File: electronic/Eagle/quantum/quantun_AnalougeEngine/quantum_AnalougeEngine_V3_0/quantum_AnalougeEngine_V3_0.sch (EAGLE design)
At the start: 258 parts, among them IC1 OP275, IC2 OP275, IC3 OP275, IC4 OP275, IC6 OP275, IC8 OP275, IC9 TL072, K5 RELAY_EE2-5NU, K6 RELAY_EE2-5NU, K7 RELAY_EE2-5NU, K8 RELAY_EE2-5NU, Q1 BLM21, U1 ATMEGA2560-16AU, U10 ATMEGA328P-AU, U10_PROG 6PIN_HEADER_SMD_OPEN, U11 ATMEGA328P-AU, U11_PROG 6PIN_HEADER_SMD_OPEN, U12 ULN2003, U1_PROG MAIN_µC, U4 THAT1240, U5 ATMEGA16U2-AU, U5_PROG 6PIN_HEADER_SMD_OPEN, U6 THAT1240, U7 THAT1240, U8 THAT1240

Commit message: minor changes
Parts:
- removed C23, C24, C33, C34, C38, C39, C44, C45, C46: 22pF, C_Sager_Bibliothek:CAPACITOR"
- removed C31, C35, C40, C51: 1uF, C_Sager_Bibliothek:CAPACITOR"
- removed C32, C37, C42, C43, C47, C48, C49, C50, C52, C65, C66: 100nF, C_Sager_Bibliothek:CAPACITOR"
- removed C36, C41: 4,7uF/16V, C_Sager_Bibliothek:SMD_ELCTROLYTIC
- removed CONN1: 10PIN_HEADER_SMD, C_Sager_Bibliothek:10PIN_HEADER_SMD
- removed D10, D11, D12, D13, D14, D9: 4148, C_Sager_Bibliothek:4148
- removed DAC1, DAC2: MCP4922, SPI:MCP4922
- removed F1: FUSE_500 mA, C_Sager_Bibliothek:RESTABLE_FUSE
- removed L, L/M_OUT, M, R, R/S_OUT, S: 0R, C_Sager_Bibliothek:RESISTOR"
- removed Q1: BLM21, C_Sager_Bibliothek:FERITEFERITE
- removed QA1, QA2, QA3, QA4: 16 MHz, C_Sager_Bibliothek:CRYSTAL_SM49
- removed R35, R36, R37, R38, R39, R40: 500R, C_Sager_Bibliothek:RESISTOR"
- removed R41, R42, R43, R44: 1K, C_Sager_Bibliothek:RESISTOR"
- removed R45, R68: 1k, C_Sager_Bibliothek:RESISTOR"
- removed R46, R47: 1M, C_Sager_Bibliothek:RESISTOR"
- removed TP05, TP06, TP27, TP28, TP29, TP30, TP31, TP32, TP33, TP34, TP35: TPTHT, C_Sager_Bibliothek:TPTHT
- removed U10, U11: ATMEGA328P-AU, C_Sager_Bibliothek:ATMEGA328P-AU
- removed U10_PROG, U11_PROG, U5_PROG: 6PIN_HEADER_SMD_OPEN, C_Sager_Bibliothek:6PIN_HEADER_SMD_OPEN
- removed U1_PROG: MAIN_µC, C_Sager_Bibliothek:6PIN_HEADER_SMD_OPEN
- removed U5: ATMEGA16U2-AU, C_Sager_Bibliothek:ATMEGA16U2-AU
- removed UR1: 78, C_Sager_Bibliothek:78
- removed USB1: (no value), C_Sager_Bibliothek:SMARTPRJ_PN61729
- removed V1, V2: CG0603ML, C_Sager_Bibliothek:VARISTORVAR-0603
- added IC5: NE5532D, linear:NE5532D
- added L7, L8: SMD_LED_0603, C_Sager_Bibliothek:SMD_LED_0603
- C59, C64: value 22pF -> 100nF
- D1, D2: value Shotky-CD1206 -> 4148
- IC2, IC3, IC6: value OP275 -> NE5532D; device C_Sager_Bibliothek:OP275 -> linear:NE5532D; SPICEPREFIX (none) -> Z
- R1: value 22R -> 100k; SPICEPREFIX (none) -> R
- R13: value 0R -> 100k
- R15, R3: value 1M -> 0R
- R16, R31: value 10k -> 100k
- R17: SPICEPREFIX (none) -> R
- R19, R24: value 100k -> 0R
- R2: value 22R -> 100k
- R21, R26: value 100k -> 180k
- R30: value 10k -> 180k
- R32, R6: value 1k -> 100k
- R33: value 1M -> 500R
- R34: value 10k -> 500R
- R4: value 1M -> 100k
- R48, R49: value 10k -> 20k
- R5: value 1k -> 180k
- U1: value ATMEGA2560-16AU -> NUCLEO-F429ZI; device C_Sager_Bibliothek:ATMEGA2560-16AU -> NUCLEO-F429ZI:NUCLEO-F429ZI
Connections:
- removed net +5V(ANALOG): C52.2, C65.2, C66.2, DAC1.VDD, DAC2.VDD, R30.2, UR1.VO
- removed net C_D(+): R2.1, USB1.3, V2.1
- removed net C_D(-): R1.1, USB1.2, V1.1
- removed net C_UVCC: F1.1, USB1.1
- removed net D(+): R2.2, U5.D+
- removed net D(-): R1.2, U5.D-
- removed net DAC_REF_VOLTAGE: DAC1.V_REF_A, DAC1.V_REF_B, DAC2.V_REF_A, DAC2.V_REF_B, R30.1, R31.2, TP35.TP
- removed net L/M_OUT_SIGNAL: L/M_OUT.2, TP03.TP, U1.PF4_(ADC4/TCK), U10.PC4, U11.PC4
- removed net MAIN_µC_AREF: C50.1, U1.AREF
- removed net MAIN_µC_PB1(SCK): U1.(SCK/PCINT1)_PB1, U1_PROG.P$3
- removed net MAIN_µC_PB2(MOSI): U1.(MOSI/PCINT2)_PB2, U1_PROG.P$4
- removed net MAIN_µC_PB3(MISO): U1.(MISO/PCINT3)_PB3, U1_PROG.P$1
- removed net MAIN_µC_RESET: C43.1, C46.1, D2.A, R46.1, U1.~RESET, U1_PROG.P$5
- removed net MAIN_µC_RX0: R5.2, TP31.TP, U1.(RXD0/PCINT8)_PE0
- removed net MAIN_µC_RX1: R68.2, U1.(RXD1/INT2)_PD2
- removed net MAIN_µC_RX2: R41.2, TP27.TP, U1.(RXD2)_PH0
- removed net MAIN_µC_RX3: R43.2, TP33.TP, U1.PJ0_(RXD3/PCINT9)
- removed net MAIN_µC_TX0: R6.2, TP32.TP, U1.(TXD0)_PE1
- removed net MAIN_µC_TX1: R32.2, U1.(TXD1/INT3)_PD3
- removed net MAIN_µC_TX2: R42.2, TP28.TP, U1.(TXD2)_PH1
- removed net MAIN_µC_TX3: R44.2, TP34.TP, U1.PJ1_(TXD3/PCINT10)
- removed net MAIN_µC_XTAL1: C44.2, QA4.2, R47.2, U1.XTAL1
- removed net MAIN_µC_XTAL2: C45.2, QA4.1, R47.1, U1.XTAL2
- removed net M_SIGNAL: M.2, TP05.TP, U1.PF2_(ADC2), U10.PC2, U11.PC2
- removed net N$50: D11.C, R24.2, S.1
- removed net N$52: D12.A, D3.C, IC6A.OUT
- removed net N$53: D12.C, L/M_OUT.1, R26.2
- removed net N$54: D13.A, IC6B.-IN, R27.2, R28.1
- removed net N$55: D13.C, D14.A, IC6B.OUT
- removed net N$56: D14.C, R/S_OUT.1, R28.2
- removed net N$63: DAC1.SCK, R36.2
- removed net N$66: DAC1.SDI, R37.2
- removed net N$67: DAC2.CS, R40.2
- removed net N$68: DAC2.SCK, R39.2
- removed net N$69: DAC2.SDI, R38.2
- removed net N$74: C43.2, R45.2, U5./_HWB_/_AIN6_/_T0_/_INT7)_PD7
- removed net R/S_OUT_SIGNAL: R/S_OUT.2, TP04.TP, U1.PF5_(ADC5/TMS), U10.PC5, U11.PC5
- removed net S_SIGNAL: S.2, TP06.TP, U1.PF3_(ADC3), U10.PC3, U11.PC3
- removed net UCAP: C31.2, U5.UCAP
- removed net USB_µC_MISO: U5.PB3_(PDO_/_MISO_/_PCINT3), U5_PROG.P$1
- removed net USB_µC_MOSI: U5.(PDI_/_MOSI_/_PCINT2)_PB2, U5_PROG.P$4
- removed net USB_µC_RESET: D1.A, R4.1, U5.~RESET_(PC1_/_DW), U5_PROG.P$5
- removed net USB_µC_RX: R6.1, U5.(RXD1_/_AIN1_/_INT2)_PD2
- removed net USB_µC_SCK: U5.(SCLK_/_PCINT1)_PB1, U5_PROG.P$3
- removed net USB_µC_TX: R5.1, U5.(TXD1_/_INT3)_PD3
- removed net USB_µC_UGND: C31.1, Q1.2, U5.UGND, USB1.4
- removed net USB_µC_XTAL1: C24.2, QA1.2, R3.2, U5.XTAL1
- removed net USB_µC_XTAL2: C23.2, QA1.1, R3.1, U5.(PC0)_XTAL2
- removed net UVCC: C32.1, F1.2, U5.UVCC
- removed net VCA1_A6: U10.ADC6
- removed net VCA1_A7: U10.ADC7
- removed net VCA1_AREF: C37.2, U10.AREF
- removed net VCA1_D10: U10.PB2
- removed net VCA1_D11(MOSI): R37.1, U10.PB3, U10_PROG.P$4
- removed net VCA1_D12(MISO): U10.PB4, U10_PROG.P$1
- removed net VCA1_D13(SCK): R36.1, U10.PB5, U10_PROG.P$3
- removed net VCA1_D2: R35.1, U10.PD2
- removed net VCA1_D3: U10.PD3
- removed net VCA1_D4: U10.PD4
- removed net VCA1_D5: U10.PD5
- removed net VCA1_D6: U10.PD6
- removed net VCA1_D7: U10.PD7
- removed net VCA1_D8: U10.PB0
- removed net VCA1_D9: U10.PB1
- removed net VCA1_RESET: R16.1, U10.PC6, U10_PROG.P$5
- removed net VCA1_µC_RX: R42.1, U10.PD0
- removed net VCA1_µC_TX: R41.1, U10.PD1
- removed net VCA2_A6: U11.ADC6
- removed net VCA2_A7: U11.ADC7
- removed net VCA2_AREF: C42.2, U11.AREF
- removed net VCA2_D10: U11.PB2
- removed net VCA2_D11(MOSI): R38.1, U11.PB3, U11_PROG.P$4
- removed net VCA2_D12(MISO): U11.PB4, U11_PROG.P$1
- removed net VCA2_D13(SCK): R39.1, U11.PB5, U11_PROG.P$3
- removed net VCA2_D2: R40.1, U11.PD2
- removed net VCA2_D3: U11.PD3
- removed net VCA2_D4: U11.PD4
- removed net VCA2_D5: U11.PD5
- removed net VCA2_D6: U11.PD6
- removed net VCA2_D7: U11.PD7
- removed net VCA2_D8: U11.PB0
- removed net VCA2_D9: U11.PB1
- removed net VCA2_RESET: R34.1, U11.PC6, U11_PROG.P$5
- removed net VCA2_µC_RX: R44.1, U11.PD0
- removed net VCA2_µC_TX: R43.1, U11.PD1
- removed net XTAL1_VCA1: C33.2, QA2.2, R15.2, U10.PB6
- removed net XTAL1_VCA2: C38.2, QA3.2, R33.2, U11.PB6
- removed net XTAL2_VCA1: C34.2, QA2.1, R15.1, U10.PB7
- removed net XTAL2_VCA2: C39.2, QA3.1, R33.1, U11.PB7
- new net N$10: D3.A, R20.1, R22.2
- new net N$3: D4.C, IC2A.-IN, R17.2, R22.1
- new net N$35: IC2B.OUT, R19.1, R23.2
- new net N$37: D8.C, IC3A.-IN, R18.2, R27.1
- new net N$4: D3.C, D4.A, IC2A.OUT
- net +5V: now also L7.+, L8.+; no longer C19.1, C20.1, C35.2, C36.+, C40.2, C41.+, C47.1, C48.1, C49.1, CONN1.P$1, CONN1.P$2, CONN1.P$3, D1.C, D2.C, DAC1.SHDN, DAC2.SHDN, R16.2, R34.2, R4.2, R46.2, U1.AVCC, U1.VCC, U1.VCC_2, U1.VCC_3, U1.VCC_4, U10.AVCC, U10.VCC, U10.VCC_2, U10_PROG.P$2, U11.AVCC, U11.VCC, U11.VCC_2, U11_PROG.P$2, U1_PROG.P$2, U5.AVCC, U5.VCC, U5_PROG.P$2
- net AGND: now also C19.2, C20.2, IC5A.+IN, IC5B.+IN; no longer C51.1, C52.1, C65.1, C66.1, DAC1.VSS, DAC2.VSS, R13.2, R31.1, UR1.GND
- net DAC1_OUT(A): no longer DAC1.V_OUT_A
- net DAC1_OUT(B): no longer DAC1.V_OUT_B
- net DAC2_OUT(A): no longer DAC2.V_OUT_A
- net DAC2_OUT(B): no longer DAC2.V_OUT_B
- net DGND: no longer C19.2, C20.2, C23.1, C24.1, C32.2, C33.1, C34.1, C35.1, C36.-, C37.1, C38.1, C39.1, C40.1, C41.-, C42.1, C44.1, C45.1, C46.2, C47.2, C48.2, C49.2, C50.2, CONN1.P$10, CONN1.P$5, CONN1.P$6, CONN1.P$7, CONN1.P$8, DAC1.LDAC, DAC2.LDAC, R13.1, R45.1, U1.GND, U1.GND_2, U1.GND_3, U1.GND_4, U1.GND_5, U10.GND, U10.GND_2, U10.GND_3, U10_PROG.P$6, U11.GND, U11.GND_2, U11.GND_3, U11_PROG.P$6, U1_PROG.P$6, U5.GND, U5_PROG.P$6
- net L: now also R1.1, R21.1, R5.1
- net L/M_OUT(VCA1_OUT): no longer R25.1
- net L_SIGNAL: now also R19.2, R3.2, TP03.TP; no longer L.2, U1.PF0_(ADC0), U10.PC0, U11.PC0
- net M: no longer R21.1
- net MAIN_µC_D2: no longer U1.(OC3B/INT4)_PE4
- net MAIN_µC_D3: no longer U1.(OC3C/INT5)_PE5
- net MAIN_µC_D4: no longer U1.(OC0B)_PG5
- net MAIN_µC_D5: no longer U1.(OC3A/AIN1)_PE3
- net MAIN_µC_D6: no longer U1.(OC4A)_PH3
- net MAIN_µC_D7: no longer U1.(OC4B)_PH4
- net N$12: now also D1.A, R4.1, R6.2; no longer U1.(OC2A/PCINT4)_PB4
- net N$16: now also L3.-; no longer L2.-
- net N$20: now also IC2B.-IN, R20.2, R21.2, R23.1; no longer D5.C, L.1, R18.2
- net N$26: now also L8.-; no longer L6.-
- net N$29: now also L7.-; no longer L5.-
- net N$30: now also L6.-; no longer L4.-
- net N$32: now also L5.-; no longer L3.-
- net N$34: now also IC5B.-IN, R13.1, R4.2, R5.2; no longer Q1.1, USB1.P$1, USB1.P$2, V1.2, V2.2
- net N$36: now also IC5B.OUT, R13.2, R3.1; no longer DAC1.CS, R35.2
- net N$38: now also D5.C, D8.A, IC3A.OUT; no longer D4.A, IC2A.-IN, R17.2, R18.1
- net N$39: now also R25.1, R27.2; no longer D4.C, IC2A.OUT
- net N$40: now also IC3B.-IN, R25.2, R26.2, R28.1; no longer D6.A, IC2B.-IN, R19.2, R20.1
- net N$41: now also IC3B.OUT, R24.1, R28.2; no longer D6.C, D7.A, IC2B.OUT
- net N$42: now also IC6A.-IN, R2.2, R31.1; no longer R.1, R20.2
- net N$44: now also D6.C, D7.A, IC6A.OUT; no longer D8.A, IC3A.-IN, R21.2, R22.1
- net N$46: now also D6.A, R16.1, R31.2; no longer D8.C, D9.A, IC3A.OUT
- net N$47: now also IC6B.-IN, R16.2, R30.2, R32.1; no longer D9.C, M.1, R22.2
- net N$48: now also IC6B.OUT, R15.1, R32.2; no longer D10.A, IC3B.-IN, R23.2, R24.1
- net N$49: now also L2.-, R33.2; no longer D10.C, D11.A, IC3B.OUT
- net N$51: now also L4.-, R34.2; no longer D3.A, IC6A.-IN, R25.2, R26.1
- net N$6: now also D2.C, IC5A.-IN, R1.2, R6.1; no longer CONN1.P$4, R68.1, TP29.TP
- net N$9: now also D1.C, D2.A, IC5A.OUT; no longer CONN1.P$9, R32.1, TP30.TP
- net OUT1_DRIVER: now also R33.1
- net OUT2_DRIVER: now also R34.1
- net R: now also R18.1, R2.1, R26.1, R30.1; no longer R19.1
- net R/S_OUT(VCA2_OUT): no longer R27.1
- net R_SIGNAL: now also R15.2, R24.2, TP04.TP; no longer R.2, U1.PF1_(ADC1), U10.PC1, U11.PC1
- net S: no longer R23.1
- net V+: now also C20.1, IC5P.V+; no longer C51.2, UR1.VI
- net V-: now also C19.1, IC5P.V-
- net VCA1_EC+: no longer U1.PF7_(ADC7/TDI)
- net VCA2_EC+: no longer U1.PF6_(ADC6/TDO)
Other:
- note added: "Bypass"
- note added: "Präzisionsgleichrichter"

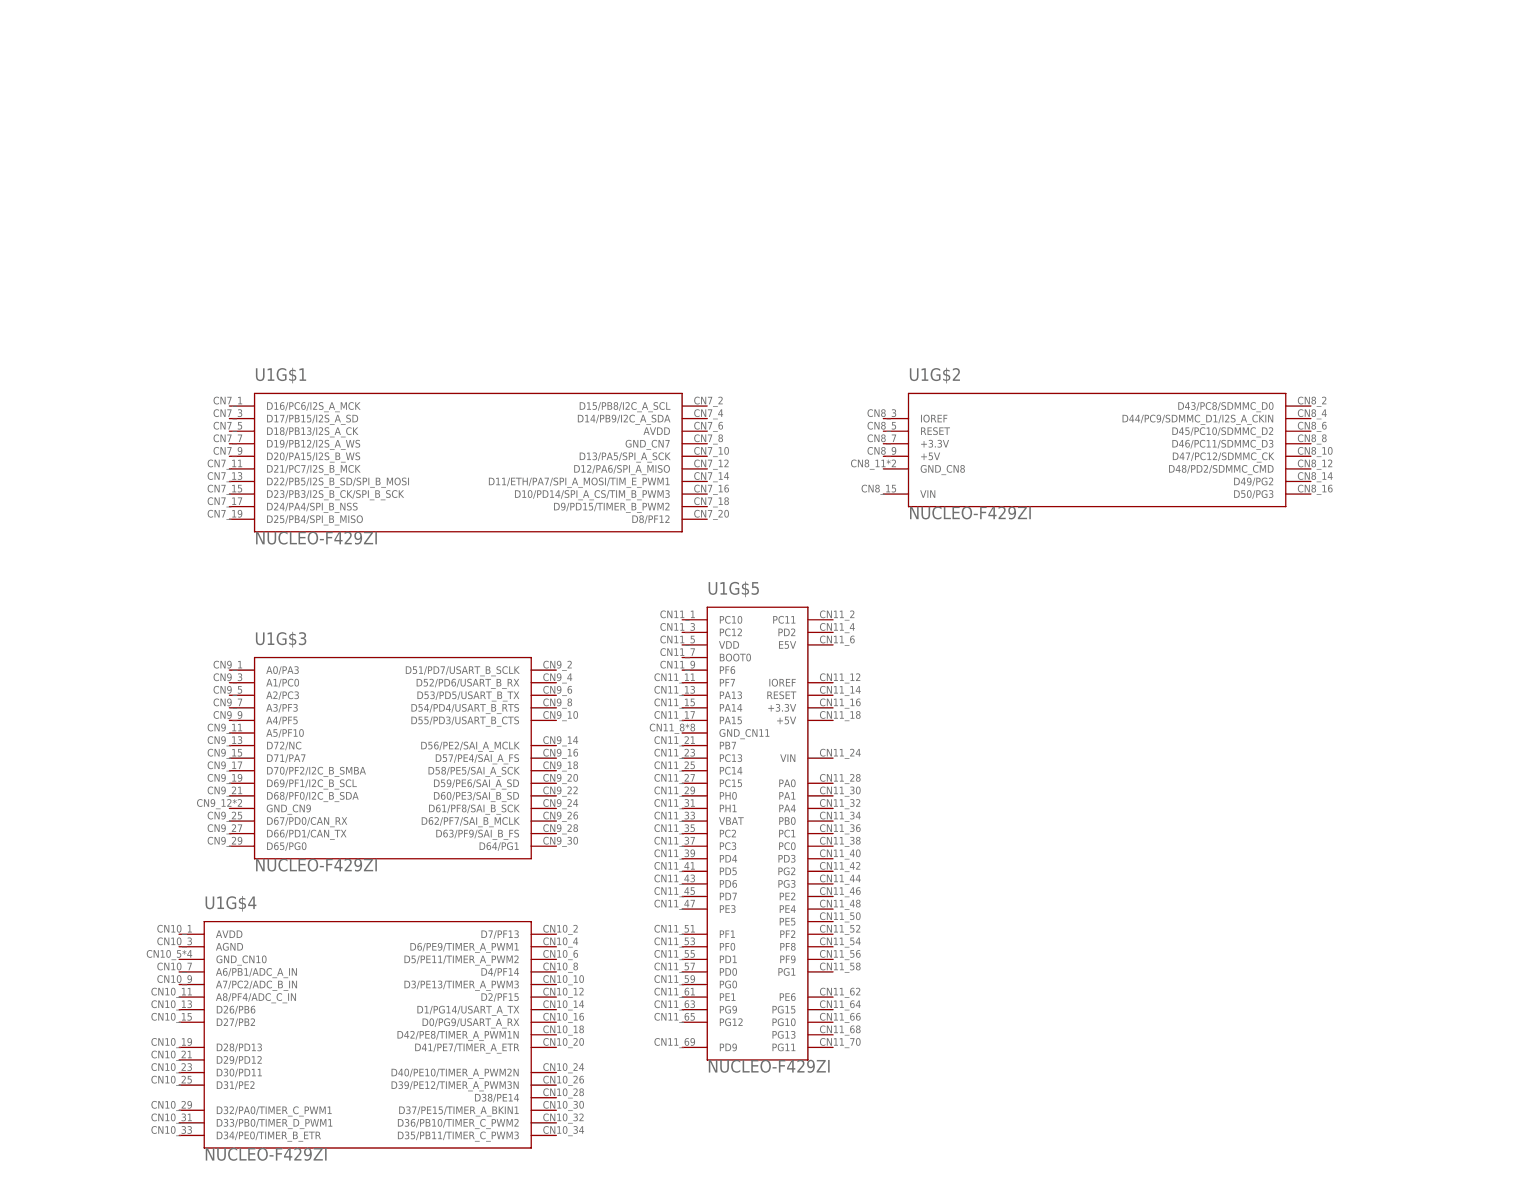
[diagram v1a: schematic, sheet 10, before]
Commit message: Shematic updates + Created MotherEngine.ioc
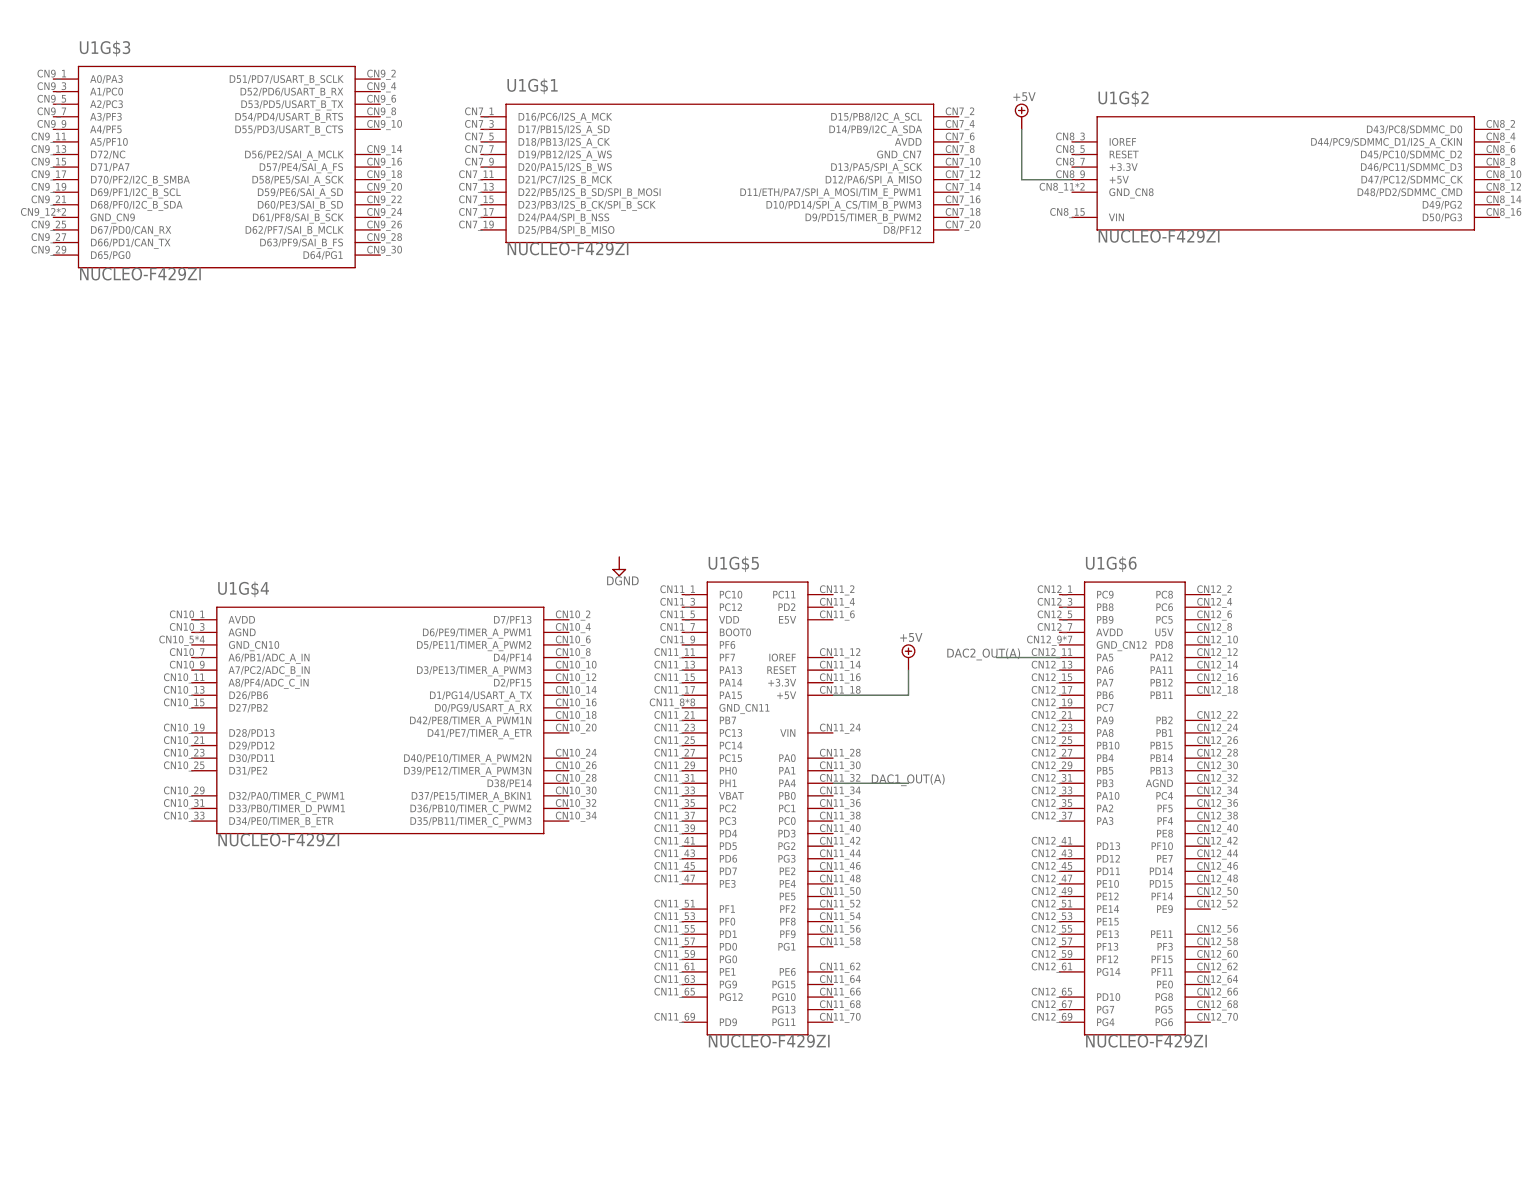
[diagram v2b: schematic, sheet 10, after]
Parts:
- removed R63, R65: 90k9, C_Sager_Bibliothek:RESISTOR"
- removed R64, R66: 51k, C_Sager_Bibliothek:RESISTOR"
- U1: device NUCLEO-F429ZI:NUCLEO-F429ZI -> STM32_144:NUCLEO-F429ZI
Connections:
- removed net DAC1_OUT(B): R64.1
- removed net DAC2_OUT(B): R66.1
- net +5V: now also U1G$2.+5V, U1G$5.+5V
- net DAC1_OUT(A): now also U1G$5.PA4
- net DAC2_OUT(A): now also U1G$6.PA5
- net N$87: no longer R63.1, R64.2
- net N$95: no longer R65.1, R66.2
- net V-: no longer R63.2, R65.2
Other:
- moved on the sheet: U1G$1, U1G$2, U1G$3, U1G$4, U1G$5

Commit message: Implemented Relais GPIOs, EAGLE Layout progress positioning (total layout job 30 %)
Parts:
- removed CONN2: (no value), C_Sager_Bibliothek:SCHRAUBKLEMME_3POL
- removed DGND1, DGND2, DGND3, DGND4, TP07, TP08, TP10, TP11, TP12, TP14, TP15, TP19, TP20, TP21, TP22, TP24, TP25, TP26: TPTHT, C_Sager_Bibliothek:TPTHT
- added R35: 0R, C_Sager_Bibliothek:RESISTOR"
- added TP05: TPTHT, C_Sager_Bibliothek:TPTHT
- added U$1: 78, C_Sager_Bibliothek:78
- added U$2, U$3: (no value), C_Sager_Bibliothek:CAPACITOR"
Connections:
- net DAC1_OUT(A) renamed DAC_OUT1
- net DAC2_OUT(A) renamed DAC_OUT2
- removed net +9V: CONN2-2.KL
- removed net MAIN_µC_D2: U12.IN1
- removed net MAIN_µC_D3: U12.IN2
- removed net MAIN_µC_D4: U12.IN3
- removed net MAIN_µC_D5: U12.IN4
- removed net MAIN_µC_D6: U12.IN5
- removed net MAIN_µC_D7: U12.IN6
- new net ADC1-IN3: U1G$6.PA3
- new net ADC1-IN6: U1G$6.PA6
- new net ADC1_IN0: U1G$5.PA0
- new net ADC2-IN10: U1G$5.PC0
- new net ADC2-IN12: U1G$5.PC2
- new net ADC2-IN9: U1G$6.PB1
- new net ADC3-IN13: U1G$5.PC3
- new net ADC3-IN14: U1G$6.PF4
- new net ADC3-IN15: U1G$6.PF5
- new net RELAIS1: U12.IN1, U1G$5.PG1
- new net RELAIS2: U12.IN2, U1G$5.PE6
- new net RELAIS3: U12.IN3, U1G$5.PG15
- new net RELAIS4: U12.IN4, U1G$5.PG10
- new net RELAIS5: U12.IN5, U1G$5.PG12
- new net RELAIS6: U12.IN6, U1G$5.PG9
- new net USART6_RX: U1G$6.PC6
- new net USRAT6_TX: U1G$6.PC7
- net +5V: now also U$1.VO, U$3.1, U1G$2.VIN; no longer CONN2-1.KL, TP07.TP, TP11.TP, TP12.TP, U1G$2.+5V, U1G$5.+5V
- net AGND: now also CONN3-1.KL, R35.1; no longer CONN3-2.KL, TP08.TP, TP14.TP, TP15.TP, TP19.TP, TP20.TP, TP21.TP, TP22.TP
- net DGND: now also R35.2, TP05.TP, U$1.GND, U$2.2, U$3.2, U1G$2.GND_CN8; no longer CONN2-3.KL, DGND1.TP, DGND2.TP, DGND3.TP, DGND4.TP
- net L/M_OUT+: now also BY_2_22.S; no longer BY_2_12.S
- net L/M_OUT-: now also BY_2_23.S; no longer BY_2_13.S
- net N$13: now also BY_2_12.S; no longer BY_2_22.S
- net N$15: now also BY_2_22.P; no longer BY_2_12.P
- net N$17: now also BY_2_23.P; no longer BY_2_13.P
- net N$25: now also BY_2_12.P; no longer BY_2_22.P
- net N$27: now also BY_2_13.P; no longer BY_2_23.P
- net N$7: now also BY_2_13.S; no longer BY_2_23.S
- net V+: now also CONN3-2.KL, U$1.VI, U$2.1; no longer CONN3-1.KL, TP24.TP, TP26.TP
- net V-: no longer TP10.TP, TP25.TP
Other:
- note added: "Analog Voltage"
- note added: "Digital Voltage"
- note added: "StarPoint"
- note removed: "nicht bestücken"
